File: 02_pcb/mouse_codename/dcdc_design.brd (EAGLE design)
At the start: 160 x 100 mm, 2 parts, among them IC1 STM32F405RGT6LQFP64

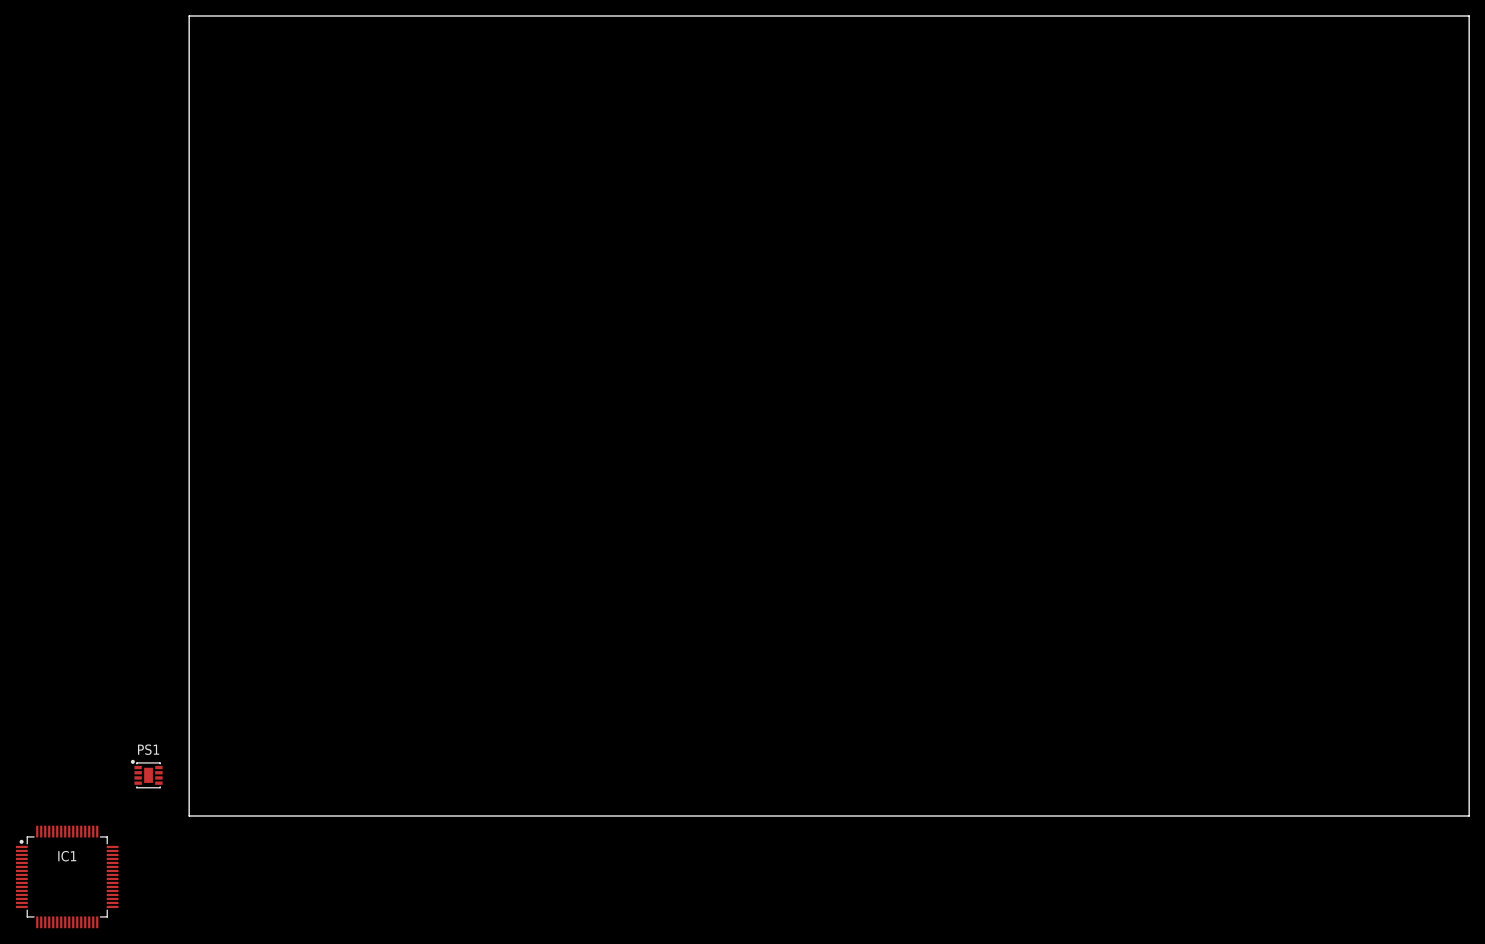
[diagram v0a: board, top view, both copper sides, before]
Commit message: eagle board layout synced with fuison 360
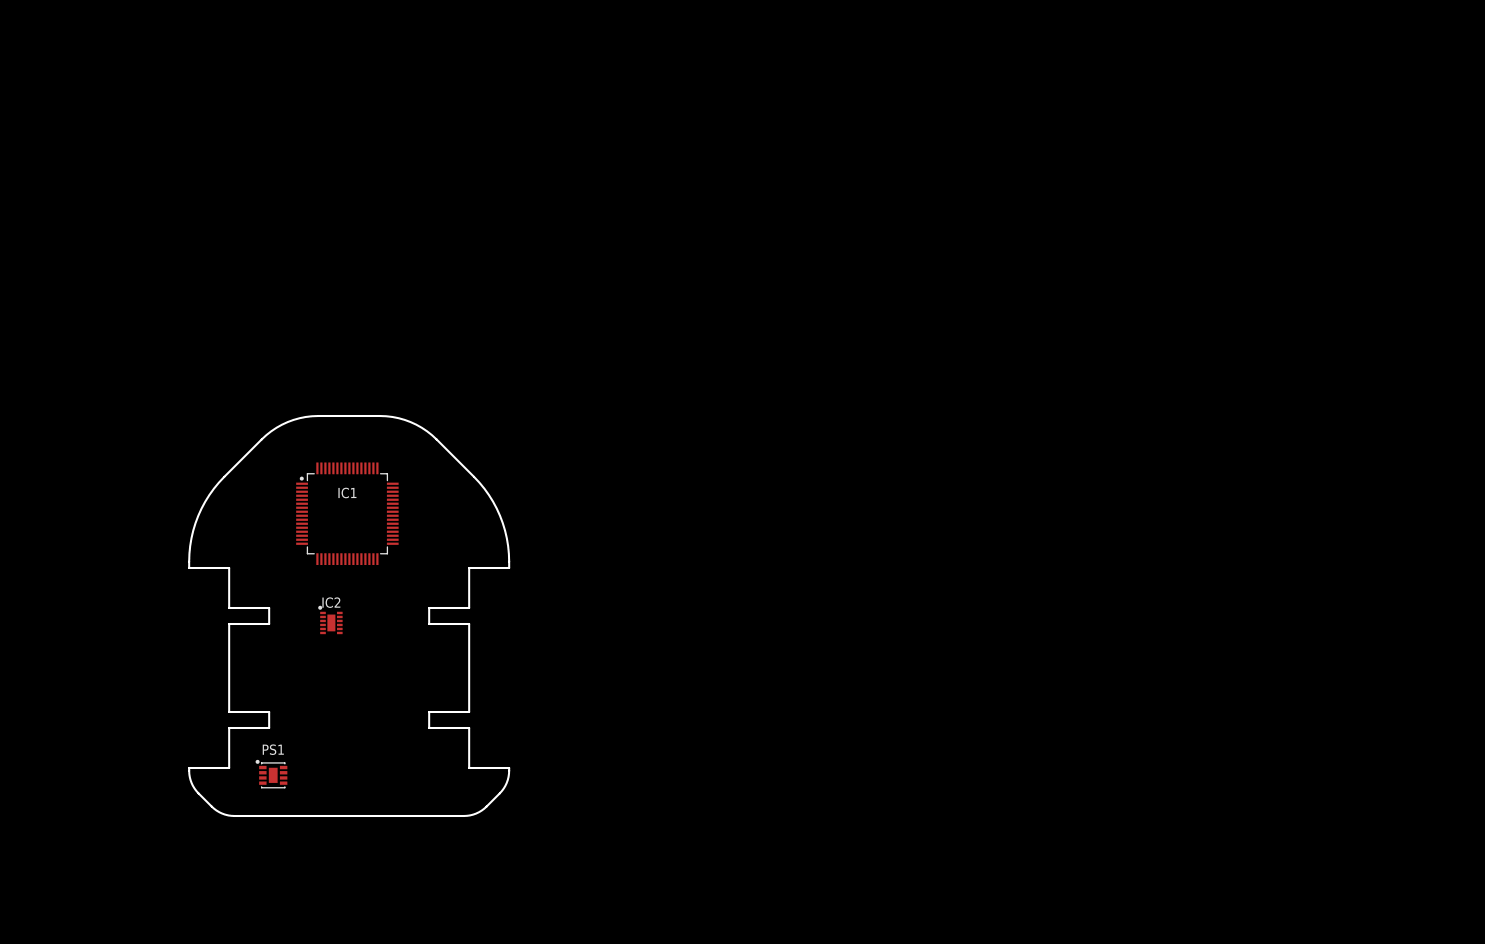
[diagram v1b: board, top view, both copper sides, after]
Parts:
- added IC2: DRV8836, SamacSys_Parts:SON50P200X300X80-13N
- IC1: value STM32F405RGT6LQFP64 -> STM32F405RG
- PS1: value TPS82085SILRSON65P280X300X133-9T -> TPS82085
- moved IC1 57.3 mm to (19.8, 37.8)
- moved PS1 15.6 mm to (10.5, 5.08)
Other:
- board size 160 x 100 mm -> 40 x 50 mm
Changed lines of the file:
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@@
 <drawing>
 <settings>
-<setting alwaysvectorfont="no"/>
+<setting alwaysvectorfont="yes"/>
 <setting verticaltext="up"/>
 </settings>
-<grid distance="50" unitdist="mil" unit="mil" style="lines" multiple="1" display="no" altdistance="5" altunitdist="mil" altunit="mil"/>
+<grid distance="50" unitdist="mil" unit="mm" style="lines" multiple="1" display="no" altdistance="5" altunitdist="mil" altunit="mm"/>
 <layers>
 <layer number="1" name="Top" color="4" fill="1" visible="yes" active="yes"/>
@@
 </layers>
 <board>
+<fusionsync huburn="a.cGVyc29uYWw6dWUyOWUzYzUy" projecturn="a.cGVyc29uYWw6dWUyOWUzYzUyIzIwMTkwMjExMTc1NjcyODUx" f3durn="urn:adsk.wipprod:dm.lineage:jzhWZ2RJTSK-yRQwBFZECw" pcbguid="5325fb4c-c49b-47e8-91f6-13e645472180" lastpulledtime="2019-02-12T16:58:25Z" lastsyncedchangeguid="7a3a4507-61db-71b5-a7ba-709196fa8ece"/>
 <plain>
-<wire x1="0" y1="0" x2="160" y2="0" width="0" layer="20"/>
-<wire x1="160" y1="0" x2="160" y2="100" width="0" layer="20"/>
-<wire x1="160" y1="100" x2="0" y2="100" width="0" layer="20"/>
-<wire x1="0" y1="100" x2="0" y2="0" width="0" layer="20"/>
+<wire x1="4.393" y1="42.393" x2="0" y2="31.787" width="0.254" layer="20" curve="45"/>
+<wire x1="0" y1="31.787" x2="0" y2="31" width="0.254" layer="20"/>
+<wire x1="0" y1="31" x2="5" y2="31" width="0.254" layer="20"/>
+<wire x1="5" y1="31" x2="5" y2="26" width="0.254" layer="20"/>
+<wire x1="5" y1="26" x2="10" y2="26" width="0.254" layer="20"/>
+<wire x1="10" y1="26" x2="10" y2="24" width="0.254" layer="20"/>
+<wire x1="10" y1="24" x2="5" y2="24" width="0.254" layer="20"/>
+<wire x1="5" y1="24" x2="5" y2="13" width="0.254" layer="20"/>
+<wire x1="5" y1="13" x2="10" y2="13" width="0.254" layer="20"/>
+<wire x1="10" y1="13" x2="10" y2="11" width="0.254" layer="20"/>
+<wire x1="10" y1="11" x2="5" y2="11" width="0.254" layer="20"/>
+<wire x1="5" y1="11" x2="5" y2="6" width="0.254" layer="20"/>
+<wire x1="5" y1="6" x2="0" y2="6" width="0.254" layer="20"/>
+<wire x1="0" y1="6" x2="0" y2="5.657" width="0.254" layer="20"/>
+<wire x1="0" y1="5.657" x2="1.172" y2="2.828" width="0.254" layer="20" curve="45"/>
+<wire x1="1.172" y1="2.828" x2="2.828" y2="1.172" width="0.254" layer="20"/>
+<wire x1="2.828" y1="1.172" x2="5.657" y2="0" width="0.254" layer="20" curve="45"/>
+<wire x1="5.657" y1="0" x2="34.343" y2="0" width="0.254" layer="20"/>
+<wire x1="34.343" y1="0" x2="37.172" y2="1.172" width="0.254" layer="20" curve="45"/>
+<wire x1="37.172" y1="1.172" x2="38.828" y2="2.828" width="0.254" layer="20"/>
+<wire x1="38.828" y1="2.828" x2="40" y2="5.657" width="0.254" layer="20" curve="45"/>
+<wire x1="40" y1="5.657" x2="40" y2="6" width="0.254" layer="20"/>
+<wire x1="40" y1="6" x2="35" y2="6" width="0.254" layer="20"/>
+<wire x1="35" y1="6" x2="35" y2="11" width="0.254" layer="20"/>
+<wire x1="35" y1="11" x2="30" y2="11" width="0.254" layer="20"/>
+<wire x1="30" y1="11" x2="30" y2="13" width="0.254" layer="20"/>
+<wire x1="30" y1="13" x2="35" y2="13" width="0.254" layer="20"/>
+<wire x1="35" y1="13" x2="35" y2="24" width="0.254" layer="20"/>
+<wire x1="35" y1="24" x2="30" y2="24" width="0.254" layer="20"/>
+<wire x1="30" y1="24" x2="30" y2="26" width="0.254" layer="20"/>
+<wire x1="30" y1="26" x2="35" y2="26" width="0.254" layer="20"/>
+<wire x1="35" y1="26" x2="35" y2="31" width="0.254" layer="20"/>
+<wire x1="35" y1="31" x2="40" y2="31" width="0.254" layer="20"/>
+<wire x1="40" y1="31" x2="40" y2="31.787" width="0.254" layer="20"/>
+<wire x1="40" y1="31.787" x2="35.607" y2="42.393" width="0.254" layer="20" curve="45"/>
+<wire x1="35.607" y1="42.393" x2="30.929" y2="47.071" width="0.254" layer="20"/>
+<wire x1="30.929" y1="47.071" x2="23.858" y2="50" width="0.254" layer="20" curve="45"/>
+<wire x1="23.858" y1="50" x2="16.142" y2="50" width="0.254" layer="20"/>
+<wire x1="16.142" y1="50" x2="9.071" y2="47.071" width="0.254" layer="20" curve="45"/>
+<wire x1="9.071" y1="47.071" x2="4.393" y2="42.393" width="0.254" layer="20"/>
 </plain>
 <attributes>
@@
 </autorouter>
 <elements>
-<element name="PS1" library="SamacSys_Parts" package="SON65P280X300X133-9T110X190" package3d_urn="urn:adsk.eagle:package:8852109/1" value="TPS82085SILRSON65P280X300X133-9T" x="-5.08" y="5.08" smashed="yes">
-<attribute name="NAME" x="-5.08" y="7.6534" size="1.27" layer="25" align="bottom-center"/>
-<attribute name="VALUE" x="-5.08" y="2.895" size="1.27" layer="27" align="top-center"/>
+<element name="PS1" library="SamacSys_Parts" package="SON65P280X300X133-9T110X190" package3d_urn="urn:adsk.eagle:package:8852109/1" value="TPS82085" x="10.51" y="5.08" smashed="yes">
+<attribute name="NAME" x="10.51" y="7.6534" size="1.27" layer="25" align="bottom-center"/>
+<attribute name="VALUE" x="10.51" y="2.895" size="1.27" layer="27" align="top-center"/>
 </element>
-<element name="IC1" library="SamacSys_Parts" package="QFP50P1200X1200X160-64" package3d_urn="urn:adsk.eagle:package:8852219/1" value="STM32F405RGT6LQFP64" x="-15.24" y="-7.62" smashed="yes">
-<attribute name="NAME" x="-15.24" y="-5.6591" size="1.27" layer="25" align="bottom-center"/>
-<attribute name="VALUE" x="-15.24" y="-9.5809" size="1.27" layer="27" align="top-center"/>
+<element name="IC1" library="SamacSys_Parts" package="QFP50P1200X1200X160-64" package3d_urn="urn:adsk.eagle:package:8852219/1" value="STM32F405RG" x="19.78" y="37.78" smashed="yes">
+<attribute name="NAME" x="19.78" y="39.7409" size="1.27" layer="25" align="bottom-center"/>
+<attribute name="VALUE" x="19.78" y="33.2791" size="1.27" layer="27" align="top-center"/>
+</element>
+<element name="IC2" library="SamacSys_Parts" package="SON50P200X300X80-13N" value="DRV8836" x="17.78" y="24.13" smashed="yes">
+<attribute name="DESCRIPTION" value="1.5A Low Voltage Stepper or Single/Dual Brushed DC Motor Driver (PWM or PH/EN Ctrl)" x="17.78" y="24.13" size="1.778" layer="27" display="off"/>
+<attribute name="HEIGHT" value="0.8mm" x="17.78" y="24.13" size="1.778" layer="27" display="off"/>
+<attribute name="MANUFACTURER_NAME" value="Texas Instruments" x="17.78" y="24.13" size="1.778" layer="27" display="off"/>
+<attribute name="MANUFACTURER_PART_NUMBER" value="DRV8836DSSR" x="17.78" y="24.13" size="1.778" layer="27" display="off"/>
+<attribute name="MOUSER_PART_NUMBER" value="595-DRV8836DSSR" x="17.78" y="24.13" size="1.778" layer="27" display="off"/>
+<attribute name="NAME" x="17.78" y="26.67" size="1.27" layer="25" align="center"/>
+<attribute name="VALUE" x="17.78" y="21.59" size="1.27" layer="27" align="center"/>
 </element>
 </elements>
@@
 <compatibility>
 <note version="8.3" severity="warning">
+Since Version 8.3, EAGLE supports Fusion synchronisation.
+This feature will not be available in this version and saving
+the document will break the link to the Fusion PCB feature.
+</note>
+<note version="8.3" severity="warning">
 Since Version 8.3, EAGLE supports URNs for individual library

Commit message: updated eagle files
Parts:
- moved IC1 8.00 mm to (27.8, 37.8)
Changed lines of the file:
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@@
 </layers>
 <board>
-<fusionsync huburn="a.cGVyc29uYWw6dWUyOWUzYzUy" projecturn="a.cGVyc29uYWw6dWUyOWUzYzUyIzIwMTkwMjExMTc1NjcyODUx" f3durn="urn:adsk.wipprod:dm.lineage:jzhWZ2RJTSK-yRQwBFZECw" pcbguid="5325fb4c-c49b-47e8-91f6-13e645472180" lastpulledtime="2019-02-12T16:58:25Z" lastsyncedchangeguid="7a3a4507-61db-71b5-a7ba-709196fa8ece"/>
+<fusionsync huburn="a.cGVyc29uYWw6dWUyOWUzYzUy" projecturn="a.cGVyc29uYWw6dWUyOWUzYzUyIzIwMTkwMjExMTc1NjcyODUx" f3durn="urn:adsk.wipprod:dm.lineage:jzhWZ2RJTSK-yRQwBFZECw" pcbguid="5325fb4c-c49b-47e8-91f6-13e645472180" lastpulledtime="2019-02-12T20:33:47Z" lastsyncedchangeguid="eace44fd-66db-2beb-f4e5-1cc507ac5d5e"/>
+<fusionteam huburn="a.cGVyc29uYWw6dWUyOWUzYzUy" projecturn="a.cGVyc29uYWw6dWUyOWUzYzUyIzIwMTkwMjExMTc1NjcyODUx" folderUrn="urn:adsk.wipprod:fs.folder:co.RxKyY8RMSu-esEzEsS3Adw" urn="urn:adsk.wipprod:dm.lineage:1s2wRtowRW-Z3f7mGxVljQ"  versionUrn="urn:adsk.wipprod:fs.file:vf.1s2wRtowRW-Z3f7mGxVljQ?version=1" camFileUrn="" camFileVersionUrn="" lastpublishedchangeguid="77a21d4d-c299-4095-9b09-cffeb97aa64f"/>
 <plain>
+<wire x1="9.071" y1="47.071" x2="4.393" y2="42.393" width="0.254" layer="20"/>
 <wire x1="4.393" y1="42.393" x2="0" y2="31.787" width="0.254" layer="20" curve="45"/>
 <wire x1="0" y1="31.787" x2="0" y2="31" width="0.254" layer="20"/>
@@
 <wire x1="23.858" y1="50" x2="16.142" y2="50" width="0.254" layer="20"/>
 <wire x1="16.142" y1="50" x2="9.071" y2="47.071" width="0.254" layer="20" curve="45"/>
-<wire x1="9.071" y1="47.071" x2="4.393" y2="42.393" width="0.254" layer="20"/>
 </plain>
 <attributes>
@@
 <attribute name="VALUE" x="10.51" y="2.895" size="1.27" layer="27" align="top-center"/>
 </element>
-<element name="IC1" library="SamacSys_Parts" package="QFP50P1200X1200X160-64" package3d_urn="urn:adsk.eagle:package:8852219/1" value="STM32F405RG" x="19.78" y="37.78" smashed="yes">
-<attribute name="NAME" x="19.78" y="39.7409" size="1.27" layer="25" align="bottom-center"/>
-<attribute name="VALUE" x="19.78" y="33.2791" size="1.27" layer="27" align="top-center"/>
+<element name="IC1" library="SamacSys_Parts" package="QFP50P1200X1200X160-64" package3d_urn="urn:adsk.eagle:package:8852219/1" value="STM32F405RG" x="27.78" y="37.78" smashed="yes">
+<attribute name="NAME" x="27.78" y="39.7409" size="1.27" layer="25" align="bottom-center"/>
+<attribute name="VALUE" x="27.78" y="33.2791" size="1.27" layer="27" align="top-center"/>
 </element>
 <element name="IC2" library="SamacSys_Parts" package="SON50P200X300X80-13N" value="DRV8836" x="17.78" y="24.13" smashed="yes">

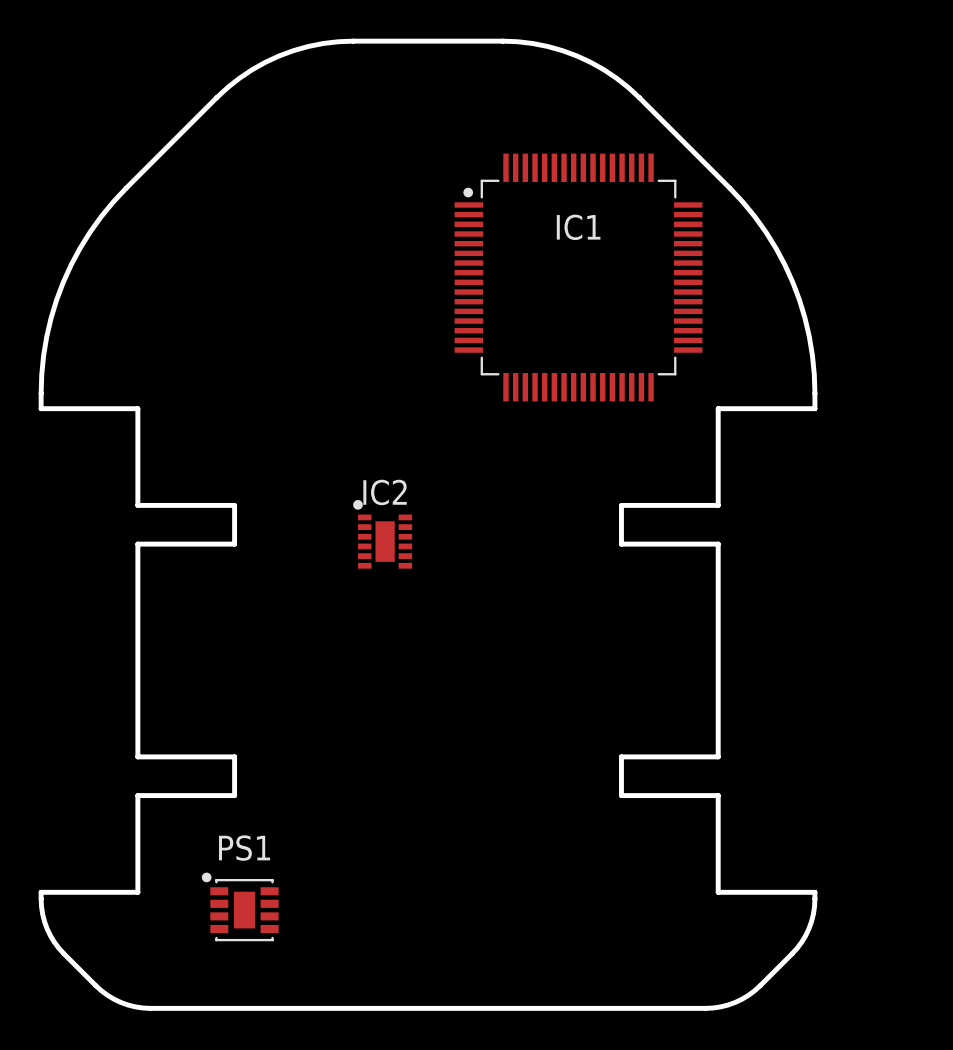
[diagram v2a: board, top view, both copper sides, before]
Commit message: pcb updated library added
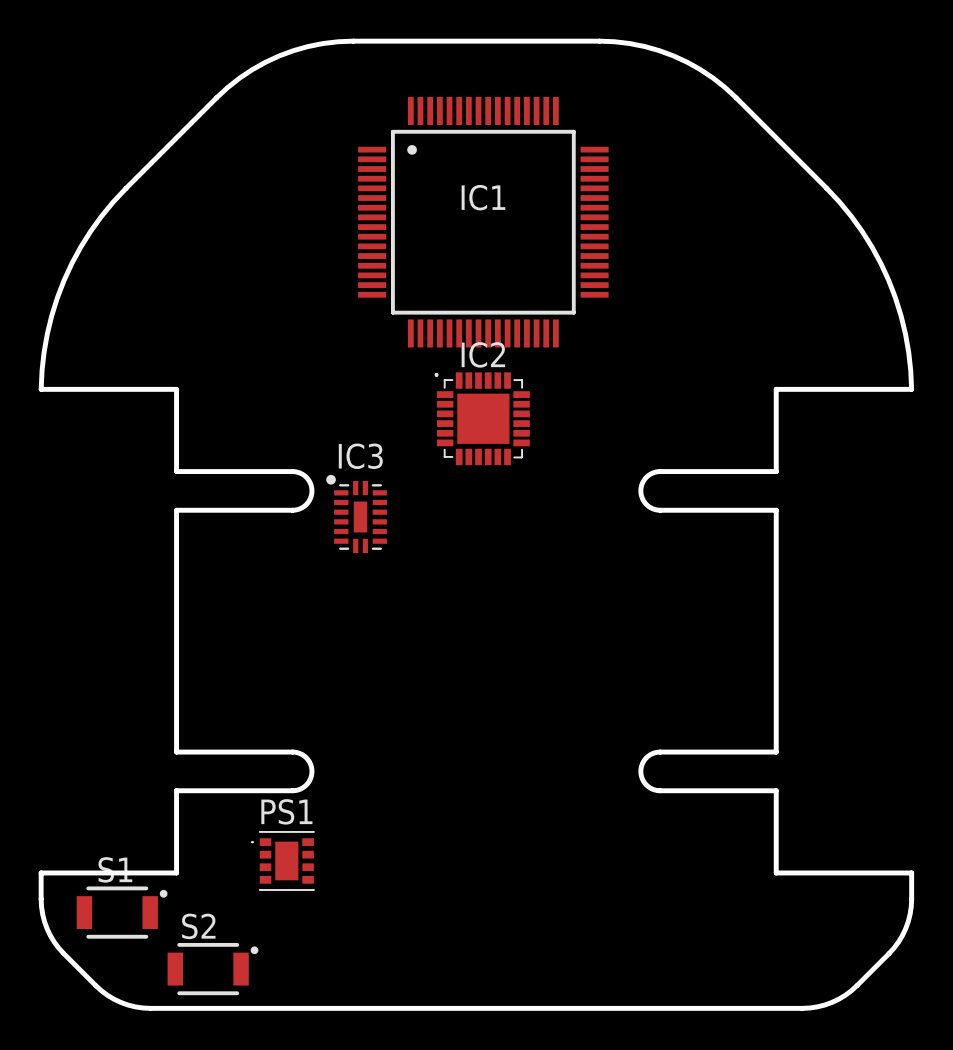
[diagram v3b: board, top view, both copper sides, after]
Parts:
- added IC3: DRV88361, parts:DRV8836
- added S1: B3U-1000P, parts:B3U-1000P
- added S2: B3U-3000PB3U-3000P, parts:B3U-3000P
- IC1: value STM32F405RG -> STM32F405RGT6; device SamacSys_Parts:QFP50P1200X1200X160-64 -> parts:QFP50P1200X1200X160-64N
- IC2: value DRV8836 -> MPU-6050; device SamacSys_Parts:SON50P200X300X80-13N -> parts:MPU6050
- PS1: device SamacSys_Parts:SON65P280X300X133-9T110X190 -> parts:TPS82085
- moved IC2 8.13 mm to (22.9, 30.5)
- moved IC1 5.69 mm to (22.9, 40.6)
- moved PS1 3.35 mm to (12.7, 7.62)
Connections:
- removed net GND_1: PS1.5
- removed net GND_2: PS1.6
- removed net VIN_1: PS1.3
- removed net VIN_2: PS1.4
- removed net VOUT: PS1.8
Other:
- board size 40 x 50 mm -> 45 x 50 mm
